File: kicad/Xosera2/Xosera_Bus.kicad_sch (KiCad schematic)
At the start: 31 parts, among them IC6 74HCT74, J1 Conn_02x05_Odd_Even, J1 Conn_02x32_Odd_Even, J2 Conn_02x07_Odd_Even, J6 Conn_01x06_Male, Q1 2N3904, U10 TXB0108DQSR, U9 TXB0108DQSR

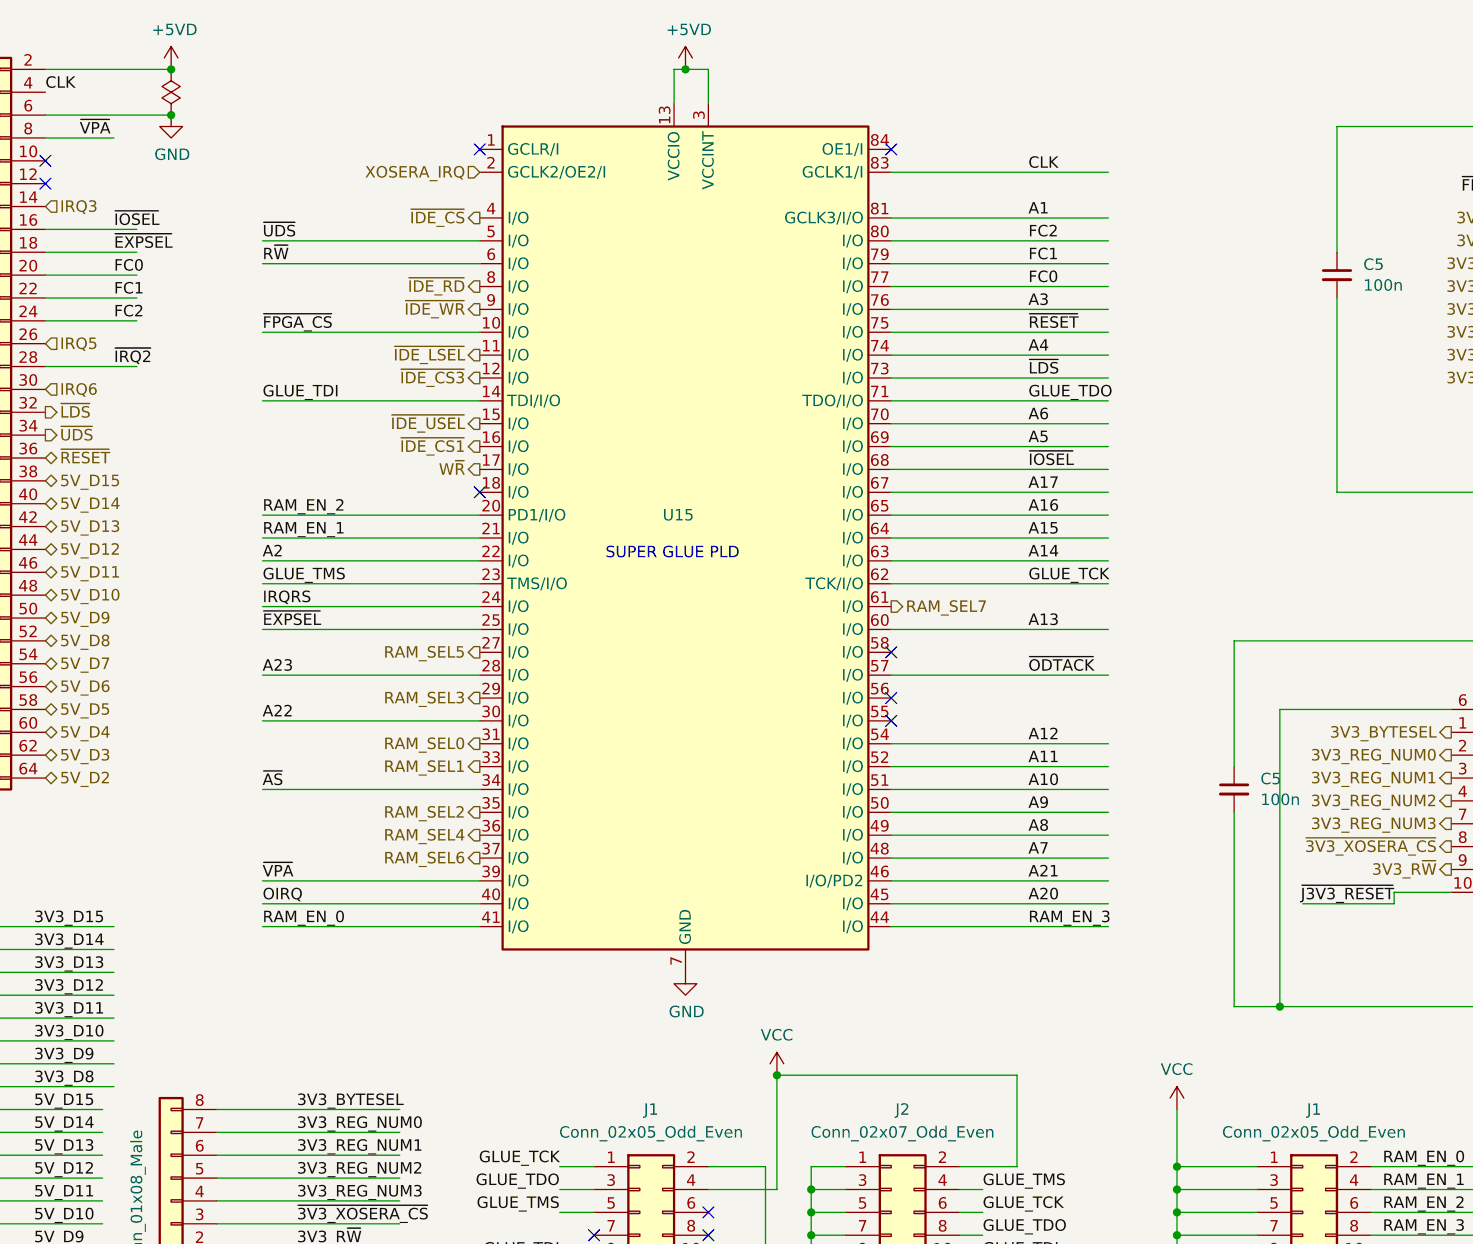
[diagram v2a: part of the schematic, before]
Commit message: Fix ERC (mostly) and sort out footprints etc
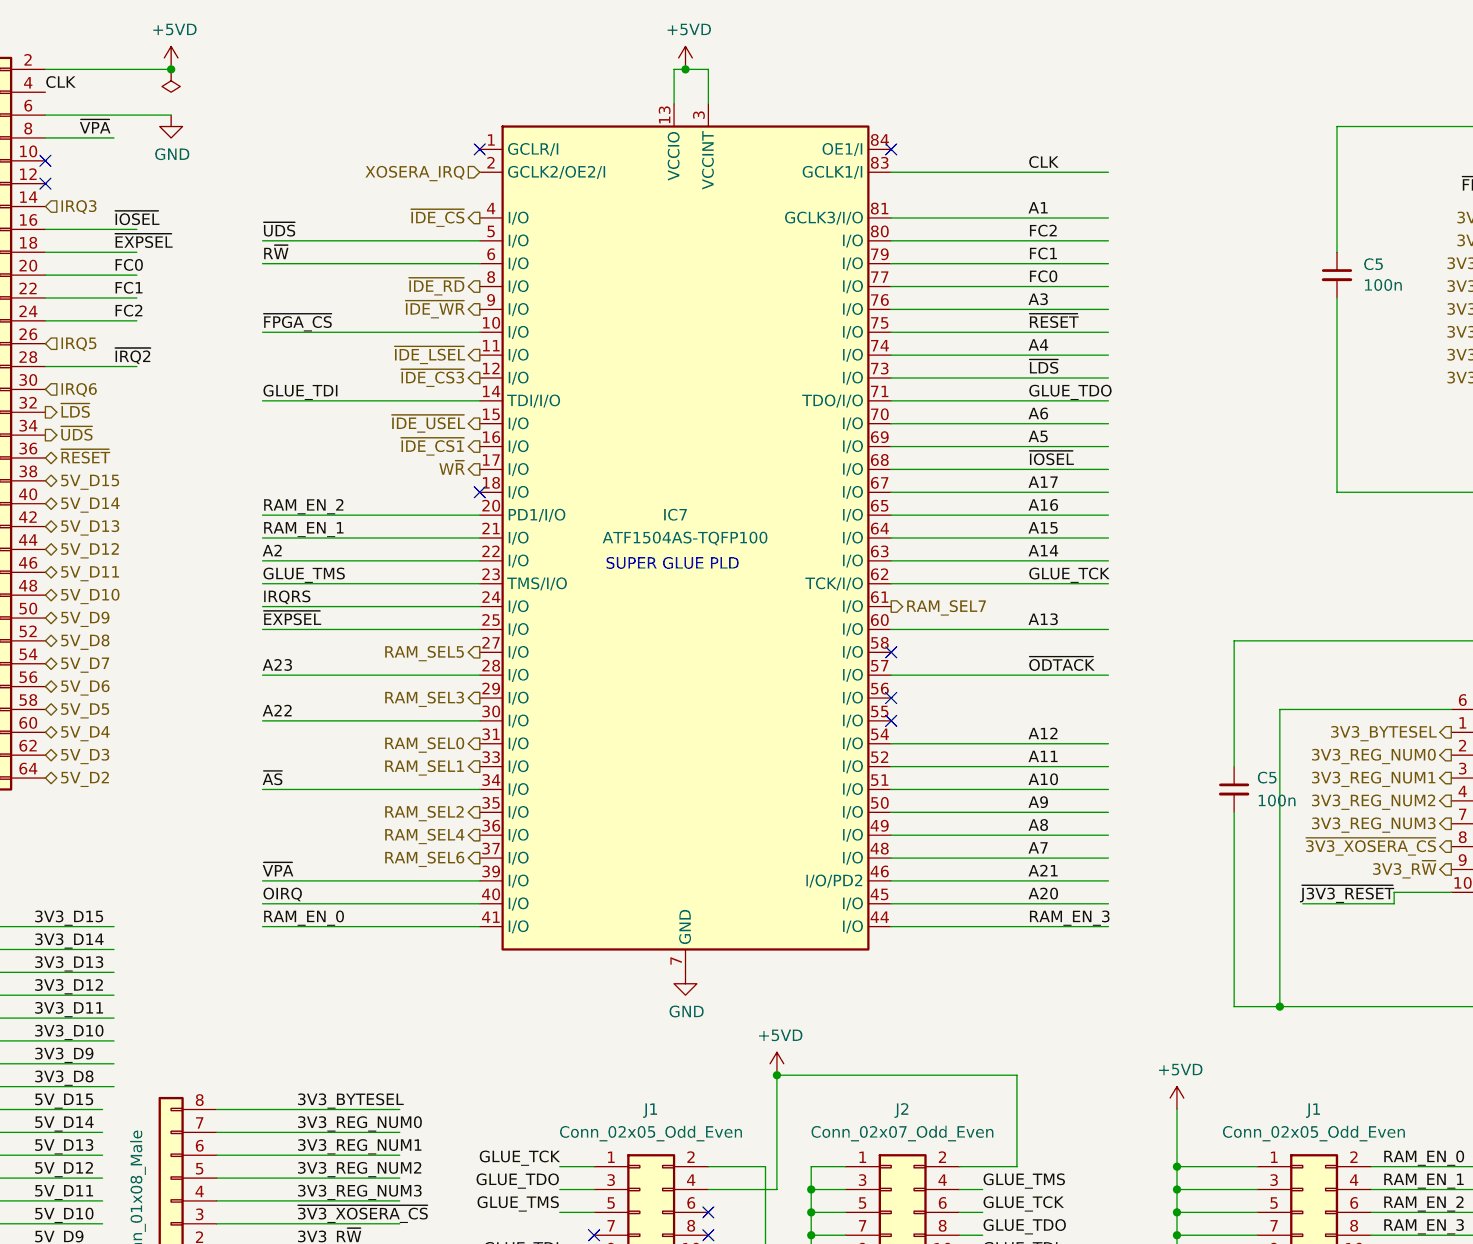
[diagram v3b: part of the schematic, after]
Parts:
- IC7: renamed from U15; value ~ -> ATF1504AS-TQFP100; footprint (none) -> Package_QFP:TQFP-100_14x14mm_P0.5mm
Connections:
- net VCC is gone; now on net +5V: J1.1 (Pin_1), J1.3 (Pin_3), J1.4 (Pin_4), J1.5 (Pin_5), J1.7 (Pin_7), J1.9 (Pin_9), J2.2 (Pin_2)
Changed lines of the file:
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@@
   (junction (at 20.32 170.18) (diameter 0) (color 0 0 0 0)
   )
-  (junction (at 118.11 132.08) (diameter 0) (color 0 0 0 0)
-  )
   (junction (at 69.85 170.18) (diameter 0) (color 0 0 0 0)
   )
@@
   (junction (at 212.09 160.02) (diameter 0) (color 0 0 0 0)
   )
-  (junction (at 50.8 25.4) (diameter 0) (color 0 0 0 0)
-  )
   (junction (at 121.92 152.4) (diameter 0) (color 0 0 0 0)
   )
@@
   (junction (at 121.92 147.32) (diameter 0) (color 0 0 0 0)
   )
+  (junction (at 118.11 132.08) (diameter 0) (color 0 0 0 0)
+  )
   (junction (at 242.57 140.97) (diameter 0) (color 0 0 0 0)
   )
@@
     (stroke (width 0) (type default))
   )
-  (text "SUPER GLUE PLD" (at 99.06 74.93 0)
+  (text "SUPER GLUE PLD" (at 99.06 76.2 0)
     (effects (font (size 1.27 1.27)) (justify left bottom))
   )
@@
   (symbol (lib_id "Device:C_Small") (at 168.91 100.33 0) (unit 1)
     (in_bom yes) (on_board yes) (dnp no)
-    (property "Reference" "C5" (at 171.831 99.1616 0)
+    (property "Reference" "C5" (at 171.45 99.06 0)
       (effects (font (size 1.27 1.27)) (justify left))
     )
-    (property "Value" "100n" (at 171.831 101.473 0)
+    (property "Value" "100n" (at 171.45 101.6 0)
       (effects (font (size 1.27 1.27)) (justify left))
     )
@@
   (symbol (lib_id "CPLD_Microchip:ATF1504AS-PLCC84") (at 107.95 72.39 0) (unit 1)
     (in_bom yes) (on_board yes) (dnp no)
-    (property "Reference" "U15" (at 105.41 69.85 0)
+    (property "Reference" "IC7" (at 105.41 69.85 0)
       (effects (font (size 1.27 1.27)) (justify left))
     )
-    (property "Value" "~" (at 107.95 50.8 0)
+    (property "Value" "ATF1504AS-TQFP100" (at 107.95 72.39 0)
       (effects (font (size 1.27 1.27)))
     )
-    (property "Footprint" "" (at 107.95 50.8 0)
+    (property "Footprint" "Package_QFP:TQFP-100_14x14mm_P0.5mm" (at 107.95 50.8 0)
       (effects (font (size 1.27 1.27)) hide)
     )
-    (property "Datasheet" "" (at 107.95 50.8 0)
+    (property "Datasheet" "https://ww1.microchip.com/downloads/en/DeviceDoc/Atmel-0950-CPLD-ATF1504AS(L)-Datasheet.pdf" (at 107.95 50.8 0)
       (effects (font (size 1.27 1.27)) hide)
     )
@@
       (project "Xosera2"
         (path "/e3ab5ddd-7cd3-46c7-91c9-5fc78e7ae4ac/0538ee98-bc97-42b9-b611-c13da646eabf"
-          (reference "U15") (unit 1)
+          (reference "IC7") (unit 1)
         )
       )
@@
     )
   )
+  (symbol (lib_id "power:+5V") (at 118.11 132.08 0) (unit 1)
+    (in_bom yes) (on_board yes) (dnp no)
+    (property "Reference" "#PWR064" (at 118.11 135.89 0)
+      (effects (font (size 1.27 1.27)) hide)
+    )
+    (property "Value" "+5VD" (at 118.491 127.6858 0)
+      (effects (font (size 1.27 1.27)))
+    )
+    (property "Footprint" "" (at 118.11 132.08 0)
+      (effects (font (size 1.27 1.27)) hide)
+    )
+    (property "Datasheet" "" (at 118.11 132.08 0)
+      (effects (font (size 1.27 1.27)) hide)
+    )
+    (pin "1")
+    (instances
+      (project "UPduino_v3.0"
+        (path "/0a0223e0-d287-426a-af6a-2d9597a86d6d"
+          (reference "#PWR064") (unit 1)
+        )
+      )
+      (project "Xosera2"
+        (path "/e3ab5ddd-7cd3-46c7-91c9-5fc78e7ae4ac/542e2bbe-89ea-4794-ae61-2e32ec6db8f5"
+          (reference "#PWR056") (unit 1)
+        )
+        (path "/e3ab5ddd-7cd3-46c7-91c9-5fc78e7ae4ac/0538ee98-bc97-42b9-b611-c13da646eabf"
+          (reference "#PWR0132") (unit 1)
+        )
+      )
+    )
+  )
   (symbol (lib_id "power:+3.3V") (at 279.4 22.86 0) (unit 1)
     (in_bom yes) (on_board yes) (dnp no)
@@
     )
   )
-  (symbol (lib_id "power:VCC") (at 118.11 132.08 0) (unit 1)
-    (in_bom yes) (on_board yes) (dnp no) (fields_autoplaced)
-    (property "Reference" "#PWR06" (at 118.11 135.89 0)
-      (effects (font (size 1.27 1.27)) hide)
-    )
-    (property "Value" "VCC" (at 118.11 127.635 0)
-      (effects (font (size 1.27 1.27)))
-    )
-    (property "Footprint" "" (at 118.11 132.08 0)
-      (effects (font (size 1.27 1.27)) hide)
-    )
-    (property "Datasheet" "" (at 118.11 132.08 0)
-      (effects (font (size 1.27 1.27)) hide)
-    )
-    (pin "1")
-    (instances
-      (project "ATF15xxProgBoard"
-        (path "/df2a4af7-7863-4ee5-b1cd-8c5ae93bba52"
-          (reference "#PWR06") (unit 1)
-        )
-      )
-      (project "Xosera2"
-        (path "/e3ab5ddd-7cd3-46c7-91c9-5fc78e7ae4ac/0538ee98-bc97-42b9-b611-c13da646eabf"
-          (reference "#PWR0103") (unit 1)
-        )
-      )
-    )
-  )
   (symbol (lib_id "Connector_Generic:Conn_02x05_Odd_Even") (at 176.53 147.32 0) (unit 1)
     (in_bom yes) (on_board yes) (dnp no) (fields_autoplaced)
@@
     )
   )
-  (symbol (lib_id "power:VCC") (at 162.56 135.89 0) (unit 1)
-    (in_bom yes) (on_board yes) (dnp no) (fields_autoplaced)
-    (property "Reference" "#PWR06" (at 162.56 139.7 0)
-      (effects (font (size 1.27 1.27)) hide)
-    )
-    (property "Value" "VCC" (at 162.56 131.445 0)
-      (effects (font (size 1.27 1.27)))
-    )
-    (property "Footprint" "" (at 162.56 135.89 0)
-      (effects (font (size 1.27 1.27)) hide)
-    )
-    (property "Datasheet" "" (at 162.56 135.89 0)
-      (effects (font (size 1.27 1.27)) hide)
-    )
-    (pin "1")
-    (instances
-      (project "ATF15xxProgBoard"
-        (path "/df2a4af7-7863-4ee5-b1cd-8c5ae93bba52"
-          (reference "#PWR06") (unit 1)
-        )
-      )
-      (project "Xosera2"
-        (path "/e3ab5ddd-7cd3-46c7-91c9-5fc78e7ae4ac/0538ee98-bc97-42b9-b611-c13da646eabf"
-          (reference "#PWR0157") (unit 1)
-        )
-      )
-    )
-  )
-  (symbol (lib_id "power:PWR_FLAG") (at 50.8 25.4 0) (unit 1)
-    (in_bom yes) (on_board yes) (dnp no)
-    (property "Reference" "#GND01" (at 50.8 23.495 0)
-      (effects (font (size 1.27 1.27)) hide)
-    )
-    (property "Value" "PWR_FLAG" (at 50.8 21.0058 0)
-      (effects (font (size 1.27 1.27)) hide)
-    )
-    (property "Footprint" "" (at 50.8 25.4 0)
-      (effects (font (size 1.27 1.27)) hide)
-    )
-    (property "Datasheet" "~" (at 50.8 25.4 0)
-      (effects (font (size 1.27 1.27)) hide)
-    )
-    (pin "1")
-    (instances
-      (project "xosera"
-        (path "/8dc290d5-5555-48ef-ac16-26d9c114edbd"
-          (reference "#GND01") (unit 1)
-        )
-      )
-      (project "Xosera2"
-        (path "/e3ab5ddd-7cd3-46c7-91c9-5fc78e7ae4ac"
-          (reference "#GND01") (unit 1)
-        )
-        (path "/e3ab5ddd-7cd3-46c7-91c9-5fc78e7ae4ac/0538ee98-bc97-42b9-b611-c13da646eabf"
-          (reference "#GND02") (unit 1)
-        )
-      )
-    )
-  )
   (symbol (lib_id "Device:C") (at 82.55 179.07 0) (unit 1)
     (in_bom yes) (on_board yes) (dnp no)
@@
         )
       )
+    )
+  )
+  (symbol (lib_id "power:+5V") (at 162.56 135.89 0) (unit 1)
+    (in_bom yes) (on_board yes) (dnp no)
+    (property "Reference" "#PWR064" (at 162.56 139.7 0)
+      (effects (font (size 1.27 1.27)) hide)
+    )
+    (property "Value" "+5VD" (at 162.941 131.4958 0)
+      (effects (font (size 1.27 1.27)))
+    )
+    (property "Footprint" "" (at 162.56 135.89 0)
+      (effects (font (size 1.27 1.27)) hide)
+    )
+    (property "Datasheet" "" (at 162.56 135.89 0)
+      (effects (font (size 1.27 1.27)) hide)
+    )
+    (pin "1")
+    (instances
+      (project "UPduino_v3.0"
+        (path "/0a0223e0-d287-426a-af6a-2d9597a86d6d"
+          (reference "#PWR064") (unit 1)
+        )
+      )
+      (project "Xosera2"
+        (path "/e3ab5ddd-7cd3-46c7-91c9-5fc78e7ae4ac/542e2bbe-89ea-4794-ae61-2e32ec6db8f5"
+          (reference "#PWR056") (unit 1)
+        )
+        (path "/e3ab5ddd-7cd3-46c7-91c9-5fc78e7ae4ac/0538ee98-bc97-42b9-b611-c13da646eabf"
+          (reference "#PWR0103") (unit 1)
+        )
+      )

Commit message: Initial layout, delete some useless things
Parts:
- removed TP1 (x2), TP3: Conn_01x08_Male, Connector_PinHeader_2.54mm:PinHeader_1x08_P2.54mm_Vertical, symbol Connector_Generic:Conn_01x08
- IC7: value ATF1504AS-TQFP100 -> ATF1504AS-PLCC84; footprint Package_QFP:TQFP-100_14x14mm_P0.5mm -> Package_LCC:PLCC-84_THT-Socket
- J1: footprint Connector_IDC:IDC-Header_2x05_P2.54mm_Vertical -> Connector_PinHeader_2.54mm:PinHeader_2x05_P2.54mm_Vertical
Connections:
- net +3.3V is gone; now on net +3V3: C5.1, C5.1, C5.1, J6.6 (Pin_6)
- net +5VD is gone; now on net +5V: C5.1, C5.1, U10.16 (VCCB), U9.16 (VCCB)
- net RAM_EN_0: no longer IC7.41 (I/O)
- net ~{IDE_CS} renamed ~{UART_CSA}
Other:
- note added: "Excluded from board!"
- moved on the sheet: J1, J2, R8
